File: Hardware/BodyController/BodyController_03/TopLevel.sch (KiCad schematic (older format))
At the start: 0 parts

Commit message: started serious layout
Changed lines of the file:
@@
 EESchema Schematic File Version 2
-LIBS:BodyController_03-rescue
 LIBS:power
 LIBS:device
@@
 LIBS:contrib
 LIBS:valves
+LIBS:HSD
+LIBS:micros
+LIBS:ICs
+LIBS:Connectors
 LIBS:BodyController_03-cache
 EELAYER 25 0
@@
 $Descr A4 11693 8268
 encoding utf-8
-Sheet 2 11
+Sheet 2 12
 Title ""
 Date ""
@@
 S 4050 4800 2250 1350
 U 59954716
-F0 "CAN" 98
-F1 "CAN.sch" 98
+F0 "COMMUNICATION" 98
+F1 "COMMUNICATION.sch" 98
 $EndSheet
 $Sheet
@@
 F1 "PowerRails.sch" 98
 $EndSheet
+$Sheet
+S 1150 6700 1900 800
+U 5A231AD0
+F0 "Inputs" 98
+F1 "Inputs.sch" 98
+$EndSheet
 $EndSCHEMATC

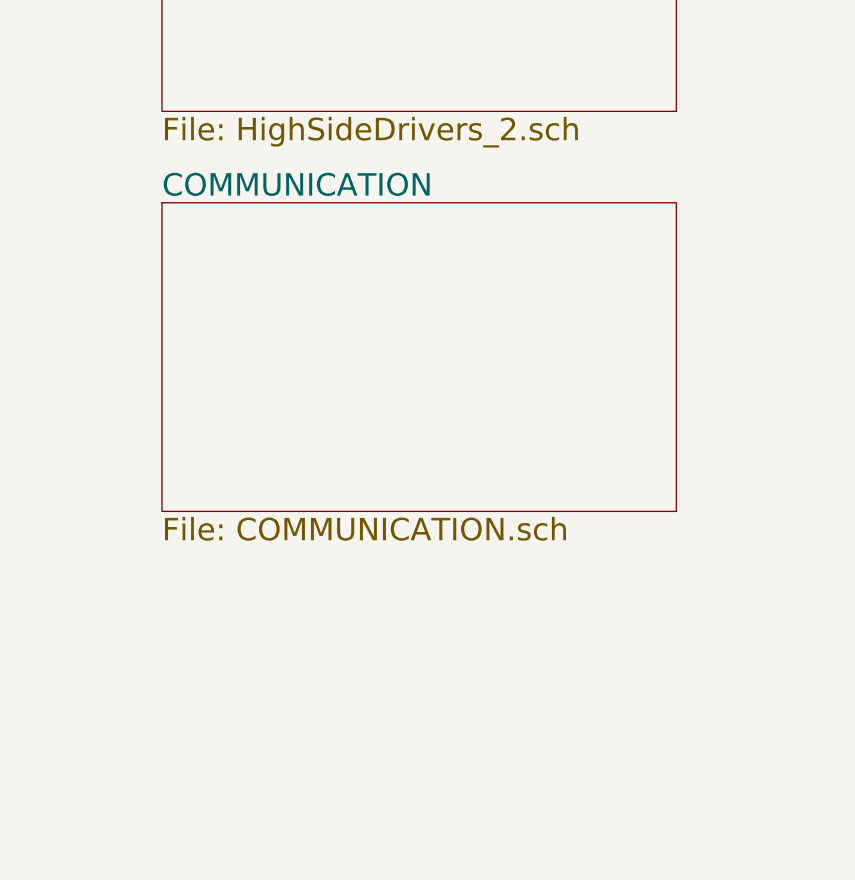
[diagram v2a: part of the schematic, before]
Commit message: Body Controller Layout Done
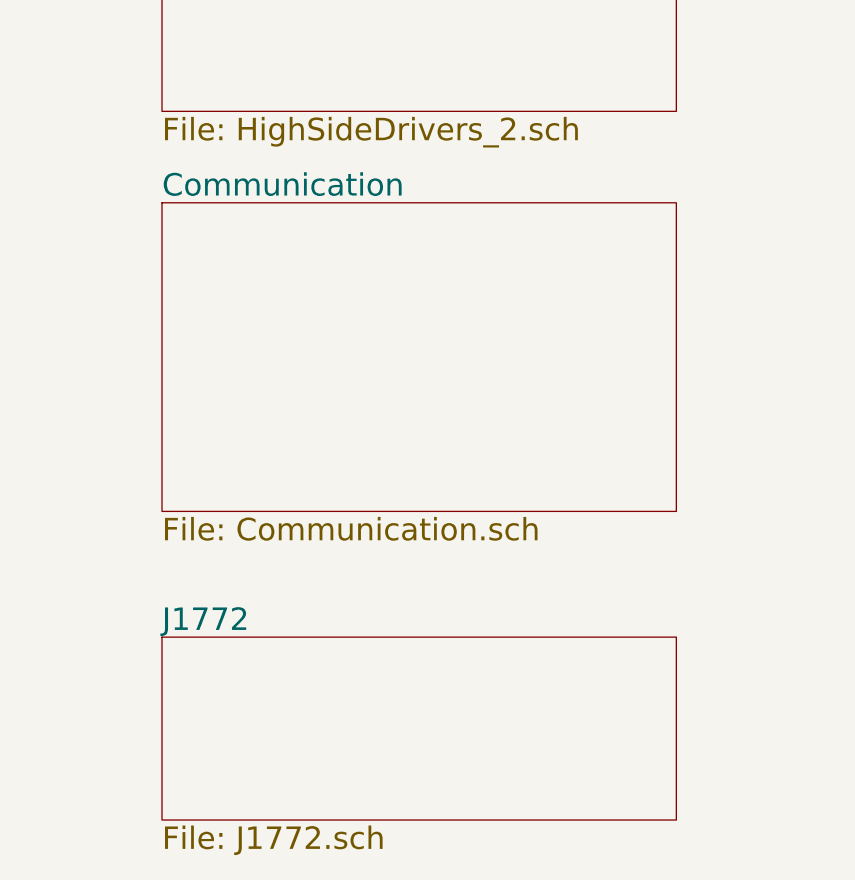
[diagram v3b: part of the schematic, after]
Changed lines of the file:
@@
 LIBS:ICs
 LIBS:Connectors
+LIBS:microchip_dspic33dsc
+LIBS:switches
 LIBS:BodyController_03-cache
 EELAYER 25 0
@@
 $Descr A4 11693 8268
 encoding utf-8
-Sheet 2 12
+Sheet 2 13
 Title ""
 Date ""
@@
 S 4050 4800 2250 1350
 U 59954716
-F0 "COMMUNICATION" 98
-F1 "COMMUNICATION.sch" 98
+F0 "Communication" 98
+F1 "Communication.sch" 98
 $EndSheet
 $Sheet
@@
 F1 "Inputs.sch" 98
 $EndSheet
+$Sheet
+S 4050 6700 2250 800
+U 5A54F298
+F0 "J1772" 98
+F1 "J1772.sch" 98
+$EndSheet
 $EndSCHEMATC
